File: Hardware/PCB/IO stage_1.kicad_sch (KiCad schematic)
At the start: 58 parts, among them IC10 THS4281DBVT, IC11 M74VHC1GT126DT1G, IC13 M74VHC1GT126DT1G, IC14 M74VHC1GT126DT1G, IC15 M74VHC1GT126DT1G, IC16 M74VHC1GT126DT1G, IC17 M74VHC1GT126DT1G, IC18 M74VHC1GT126DT1G, IC19 M74VHC1GT126DT1G, IC2 M74VHC1GT126DT1G, IC20 M74VHC1GT126DT1G, IC21 M74VHC1GT126DT1G, IC22 M74VHC1GT126DT1G, IC4 M74VHC1GT126DT1G, IC5 M74VHC1GT126DT1G, IC6 M74VHC1GT126DT1G, X1 conn 1x5 2, X10 conn 1x3, X2 conn 1x5, X3 conn 1x2, X4 conn 1x3, X5 conn 1x5, X9 conn 1x5

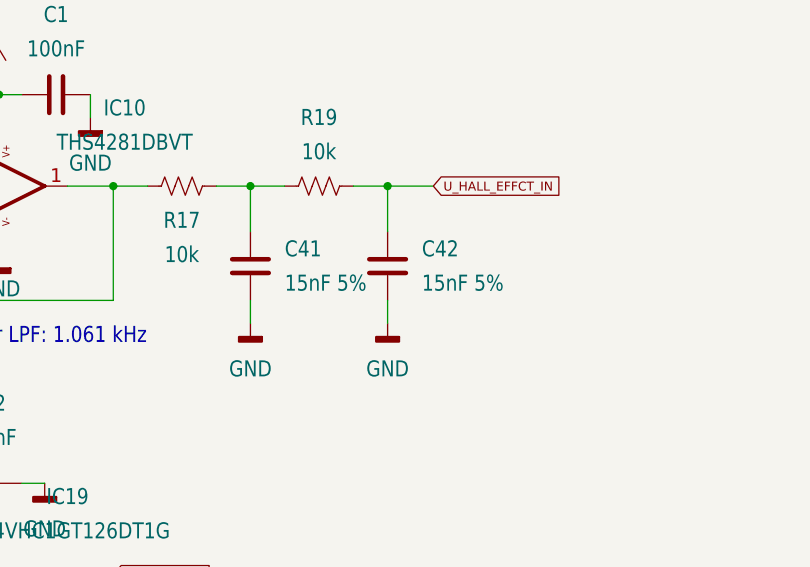
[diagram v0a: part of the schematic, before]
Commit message: MPN & OEPSPN concluded
concluded but not yet certified
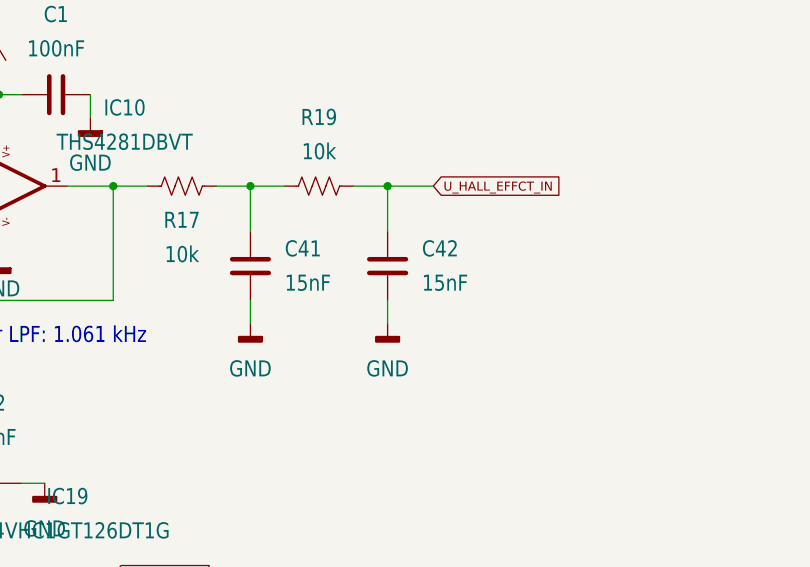
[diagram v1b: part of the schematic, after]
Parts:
- C41, C42: value 15nF 5% -> 15nF; MPN TBD 15nF 5% -> CGA2B3X7R1V153K050BB; OEPSPN (none) -> OEPS010023
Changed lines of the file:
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@@
 			)
 		)
-		(property "Value" "15nF 5%"
+		(property "Value" "15nF"
 			(at 132.08 187.325 0)
 			(effects
@@
 			)
 		)
-		(property "MPN" "TBD 15nF 5%"
+		(property "MPN" "CGA2B3X7R1V153K050BB"
 			(at 128.27 185.42 0)
 			(effects
@@
 			)
 		)
-		(property "OEPSPN" ""
+		(property "OEPSPN" "OEPS010023"
 			(at 128.27 185.42 0)
 			(effects
@@
 			)
 		)
-		(property "Value" "15nF 5%"
+		(property "Value" "15nF"
 			(at 147.32 187.325 0)
 			(effects
@@
 			)
 		)
-		(property "MPN" "TBD 15nF 5%"
+		(property "MPN" "CGA2B3X7R1V153K050BB"
 			(at 143.51 185.42 0)
 			(effects
@@
 			)
 		)
-		(property "OEPSPN" ""
+		(property "OEPSPN" "OEPS010023"
 			(at 143.51 185.42 0)
 			(effects

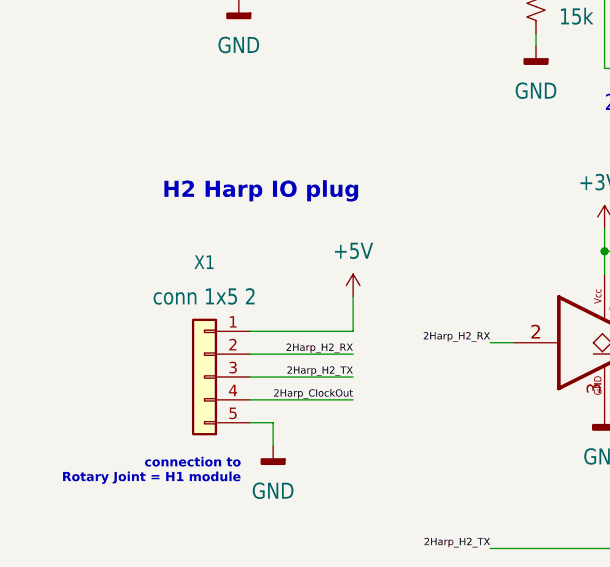
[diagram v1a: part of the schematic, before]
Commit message: fine tunning
- fine position adjust on X1 plug
- Top & Bott Fabrication Layers 'cleaned' - can be used on production
- generated new Gerbers & Drill files
- BOM & Pick&Place stand as it were
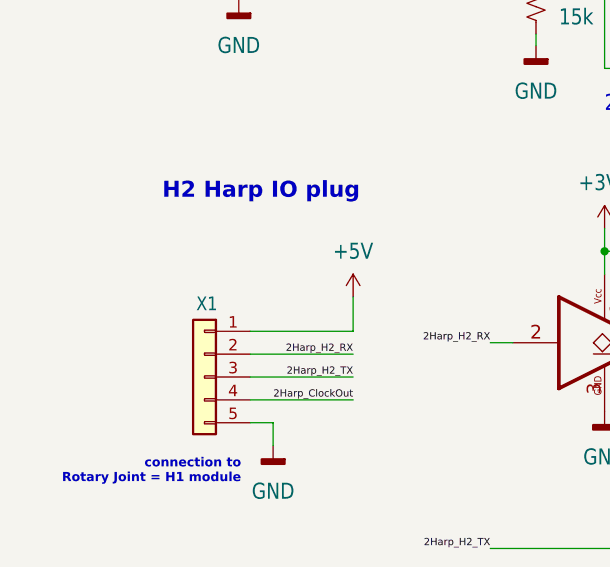
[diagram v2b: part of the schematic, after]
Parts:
- X1: footprint FastStepper PCBLib:90G-5 -> FastStepper PCBLib:20_155MH_5
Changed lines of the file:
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@@
 		(on_board yes)
 		(dnp no)
-		(fields_autoplaced yes)
 		(property "Reference" "X1"
-			(at 45.72 210.82 0)
+			(at 45.974 215.392 0)
 			(effects
 				(font
@@
 					(size 1.778 1.5113)
 				)
+				(hide yes)
 			)
 		)
-		(property "Footprint" "FastStepper PCBLib:90G-5"
+		(property "Footprint" "FastStepper PCBLib:20_155MH_5"
 			(at 45.72 223.52 0)
 			(effects

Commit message: inicio de redesenho v.1.1
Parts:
- X3: value conn 1x2 -> conn 1x3; MPN 282834-2 -> 282834-3; OEPSPN OEPS070020 -> OEPS070035
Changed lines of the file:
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@@
 			)
 		)
-		(property "Value" "conn 1x2"
+		(property "Value" "conn 1x3"
 			(at 379.095 227.33 0)
 			(effects
@@
 			)
 		)
-		(property "MPN" "282834-2"
+		(property "MPN" "282834-3"
 			(at 378.46 233.68 0)
 			(effects
@@
 			)
 		)
-		(property "OEPSPN" "OEPS070020"
+		(property "OEPSPN" "OEPS070035"
 			(at 378.46 233.68 0)
 			(effects
